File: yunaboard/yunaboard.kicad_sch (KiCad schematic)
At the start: 5 parts, among them J1 USB-C Receptable USB 2.0, U1 ESP32-S3

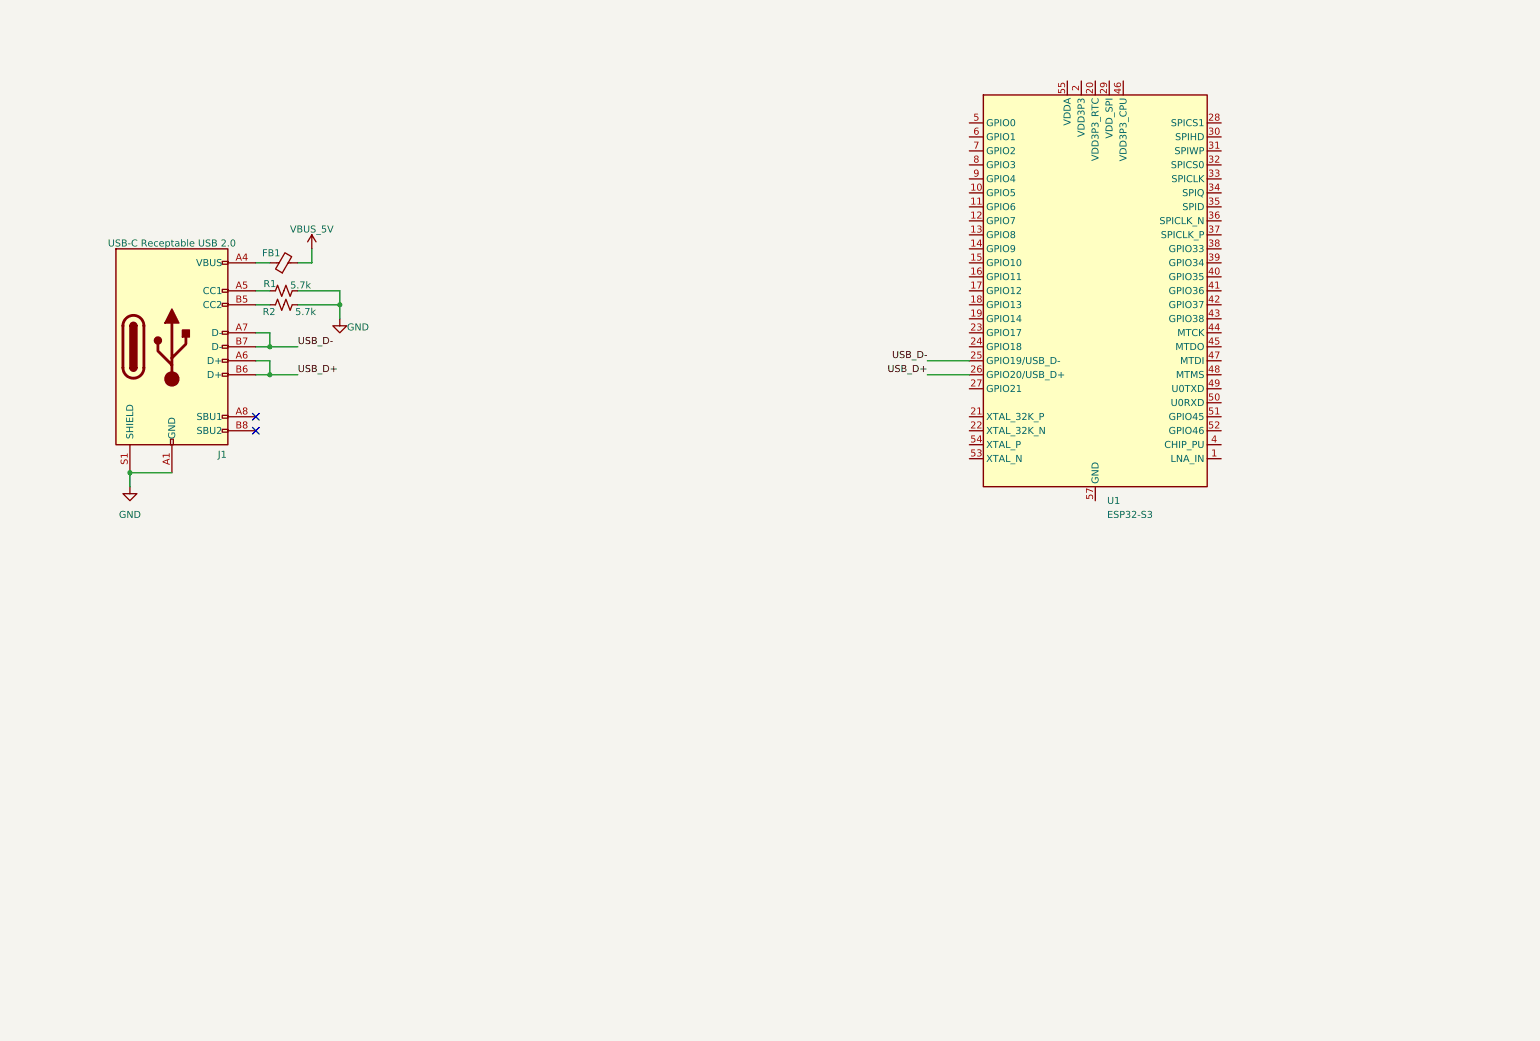
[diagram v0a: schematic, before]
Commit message: Rev 0.1
- Added initial USB-C connections
- Added ESD to USB-C data signals
- Added initial USB-to-UART bridge IC
- Added initial bulk capacitors to power inputs
- Added initial +3.3V LDO regulator
- Added initial ESP32 S3 circuitry
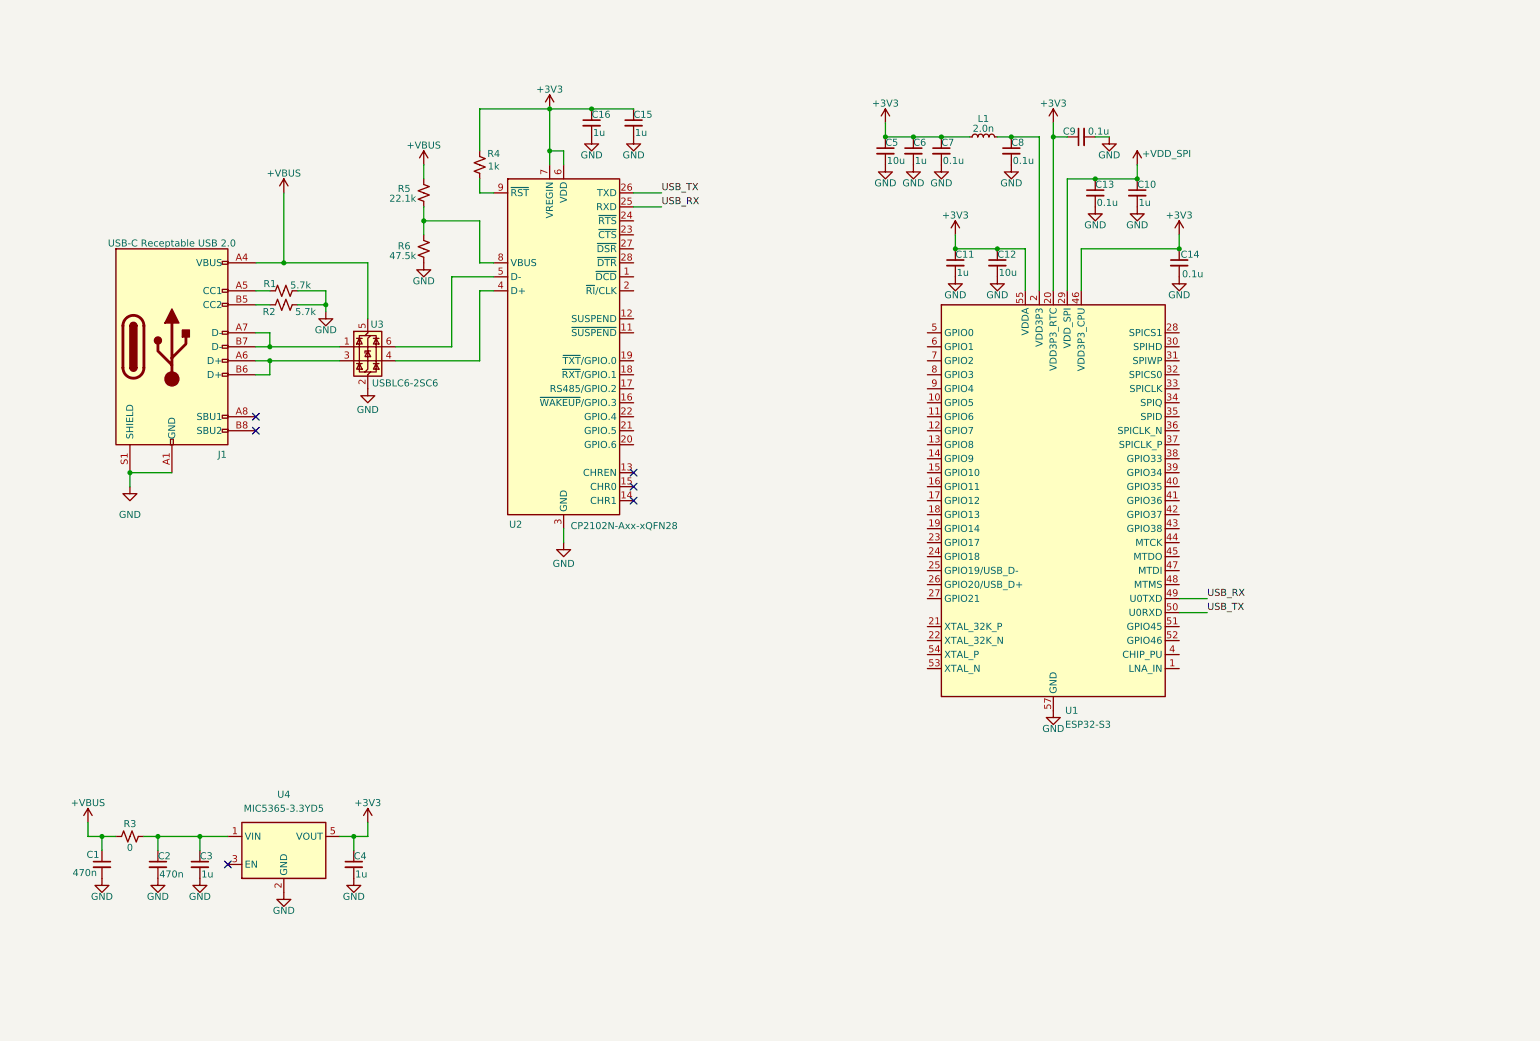
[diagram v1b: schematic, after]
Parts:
- removed FB1: FerriteBead_Small, symbol Device:FerriteBead_Small
- added C1, C2: 470n, symbol Device:C_Small
- added C10, C11, C15, C16, C3, C4, C6: 1u, symbol Device:C_Small
- added C12, C5: 10u, symbol Device:C_Small
- added C13, C14, C7, C8, C9: 0.1u, symbol Device:C_Small
- added L1: 2.0n, symbol Device:L_Small
- added R3: 0, symbol Device:R_Small_US
- added R4: 1k, symbol Device:R_Small_US
- added R5: 22.1k, symbol Device:R_Small_US
- added R6: 47.5k, symbol Device:R_Small_US
- added U2: CP2102N-Axx-xQFN28, Package_DFN_QFN:QFN-28-1EP_5x5mm_P0.5mm_EP3.35x3.35mm, symbol Interface_USB:CP2102N-Axx-xQFN28
- added U3: USBLC6-2SC6, Package_TO_SOT_SMD:SOT-23-6, symbol Power_Protection:USBLC6-2SC6
- added U4: MIC5365-3.3YD5, Package_TO_SOT_SMD:TSOT-23-5, symbol Regulator_Linear:MIC5365-3.3YD5
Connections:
- net GND: now also U1.57 (GND), C1.2, C10.2, C11.2, C12.2, C13.2, C14.2, C15.2, C16.2, C2.2, C3.2, C4.2, C5.2, C6.2, C7.2, C8.2, C9.2, R6.2, U2.29 (GND), U2.3 (GND), U3.2 (GND), U4.2 (GND)
- net +VBUS: now reaches J1.A4 (VBUS), J1.A9 (VBUS), J1.B4 (VBUS), J1.B9 (VBUS)
- net +VBUS: now also C1.1, R3.2, R5.1, U3.5 (VBUS)
- net at U1.2 (VDD3P3), U1.3 (VDD3P3): now also C8.1, L1.2
- net +3V3: now reaches U1.20 (VDD3P3_RTC)
- net +3V3: now also U1.46 (VDD3P3_CPU), U1.55 (VDDA), U1.56 (VDDA), C11.1, C12.1, C14.1, C15.1, C16.1, C4.1, C5.1, C6.1, C7.1, C9.1, L1.1, R4.1, U2.6 (VDD), U2.7 (VREGIN), U4.5 (VOUT)
- net +VDD_SPI: now reaches U1.29 (VDD_SPI)
- net +VDD_SPI: now also C10.1, C13.1
- net USB_RX: now reaches U1.49 (U0TXD)
- net USB_RX: now also U2.25 (RXD)
- net USB_TX: now reaches U1.50 (U0RXD)
- net USB_TX: now also U2.26 (TXD)
- net USB_D+: no longer names the net of J1.A6 (D+), J1.B6 (D+)
- net USB_D+: now also U3.3 (I/O2); no longer U1.26 (GPIO20/USB_D+)
- net USB_D-: no longer names the net of J1.A7 (D-), J1.B7 (D-)
- net USB_D-: now also U3.1 (I/O1); no longer U1.25 (GPIO19/USB_D-)
- new net: C2.1, C3.1, R3.1, U4.1 (VIN)
- new net: U2.4 (D+), U3.4 (I/O2)
- new net: U2.5 (D-), U3.6 (I/O1)
- new net: R5.2, R6.1, U2.8 (VBUS)
- new net: R4.2, U2.9 (~{RST})
- no-connect marks 2 -> 6
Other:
- moved on the sheet: U1

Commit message: Updated schematic
- Placed JTAG tag connect
- Placed initial circuitry to the ESP32 S3 (RF, chip PU)
- Added some labels for better readability
- Found some more documentation for the ESP32
- Added some LEDs to the USB-to-UART bridge
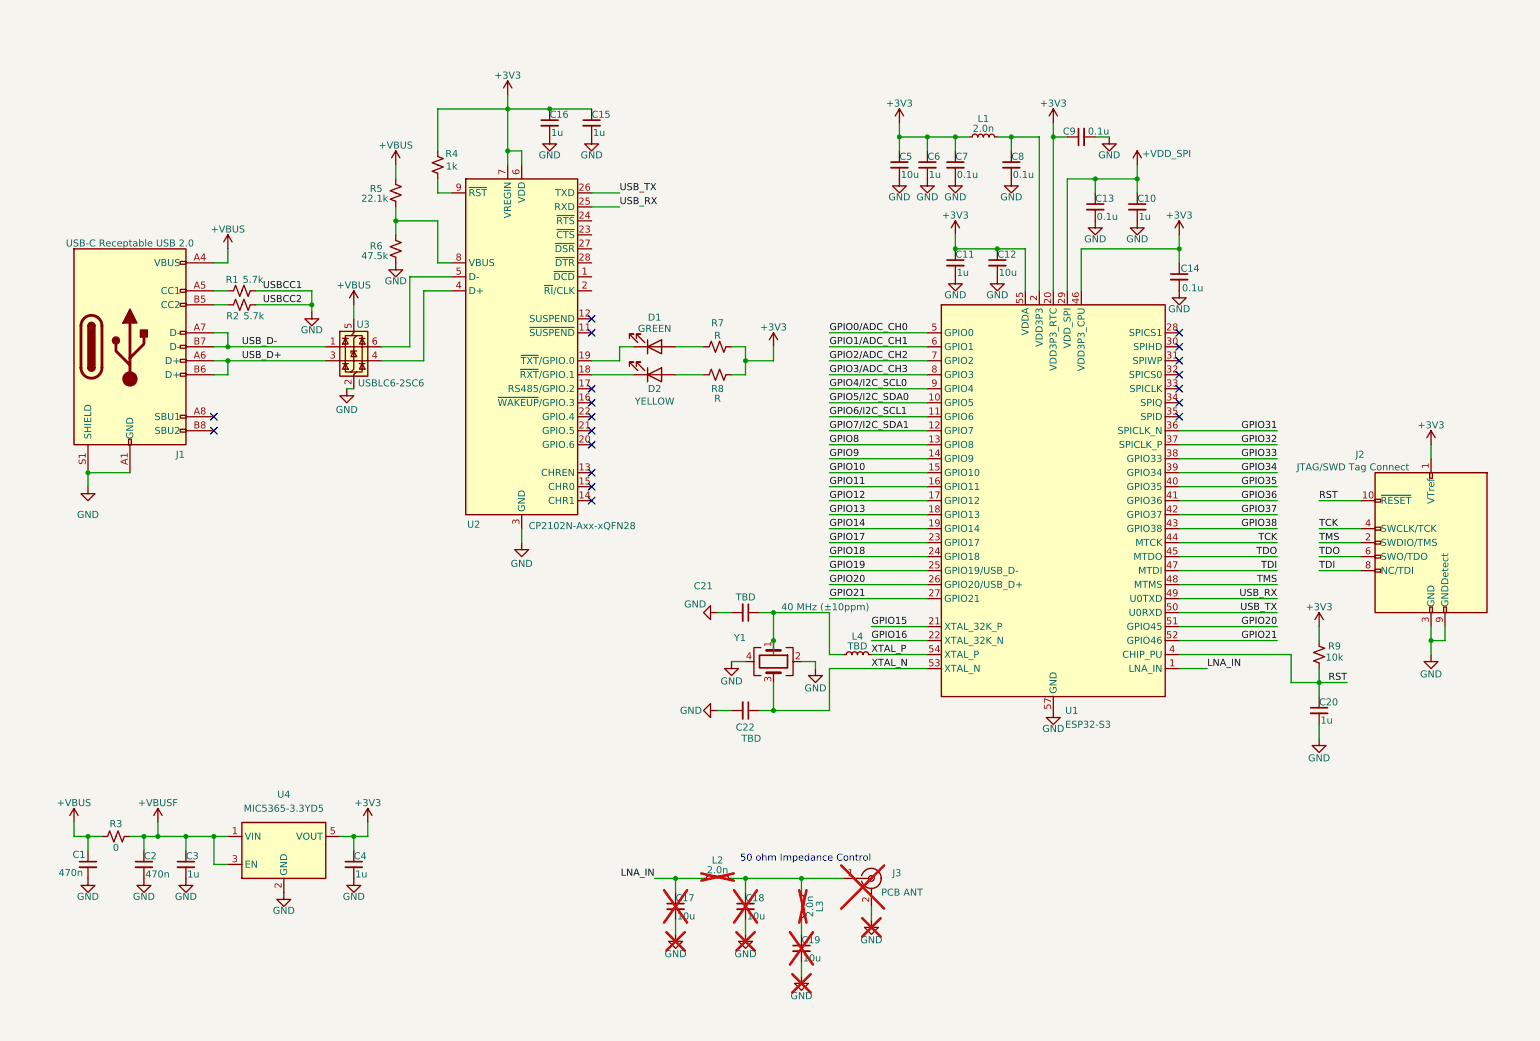
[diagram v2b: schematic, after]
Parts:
- added C17, C18, C19: 10u, symbol Device:C_Small
- added C20: 1u, symbol Device:C_Small
- added C21, C22: TBD, symbol Device:C_Small
- added D1: GREEN, symbol Device:LED
- added D2: YELLOW, symbol Device:LED
- added J2: JTAG/SWD Tag Connect, Connector:Tag-Connect_TC2070-IDC-FP_2x07_P1.27mm_Vertical, symbol Connector:Conn_ARM_JTAG_SWD_10
- added J3: PCB ANT, symbol Connector:Conn_Coaxial
- added L2, L3: 2.0n, symbol Device:L_Small
- added L4: TBD, symbol Device:L_Small
- added R7, R8: R, symbol Device:R_Small_US
- added R9: 10k, symbol Device:R_Small_US
- added Y1: 40 MHz (±10ppm), symbol Device:Crystal_GND24
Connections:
- net +3V3: now also J2.1 (VTref), R7.2, R8.2, R9.2
- net GND: now also C17.2, C18.2, C19.2, C20.2, C21.2, C22.2, J2.3 (GND), J2.5 (GND), J2.9 (GNDDetect), J3.2 (Ext), Y1.2, Y1.4
- net +VBUSF: now reaches C2.1, C3.1, R3.1, U4.1 (VIN)
- net +VBUSF: now also U4.3 (EN)
- net USB_D+: now reaches J1.A6 (D+), J1.B6 (D+), U3.3 (I/O2)
- net USB_D-: now reaches J1.A7 (D-), J1.B7 (D-), U3.1 (I/O1)
- net at U2.18 (~{RXT}/GPIO.1): now also D2.1 (K)
- net at U2.19 (~{TXT}/GPIO.0): now also D1.1 (K)
- net LNA_IN: now reaches U1.1 (LNA_IN)
- net LNA_IN: now also C17.1, L2.1
- net GPIO5/I2C_SDA0: now reaches U1.10 (GPIO5)
- net GPIO6/I2C_SCL1: now reaches U1.11 (GPIO6)
- net GPIO7/I2C_SDA1: now reaches U1.12 (GPIO7)
- net GPIO8: now reaches U1.13 (GPIO8)
- net GPIO9: now reaches U1.14 (GPIO9)
- net GPIO10: now reaches U1.15 (GPIO10)
- net GPIO11: now reaches U1.16 (GPIO11)
- net GPIO12: now reaches U1.17 (GPIO12)
- net GPIO13: now reaches U1.18 (GPIO13)
- net GPIO14: now reaches U1.19 (GPIO14)
- net GPIO15: now reaches U1.21 (XTAL_32K_P)
- net GPIO16: now reaches U1.22 (XTAL_32K_N)
- net GPIO17: now reaches U1.23 (GPIO17)
- net GPIO18: now reaches U1.24 (GPIO18)
- net GPIO19: now reaches U1.25 (GPIO19/USB_D-)
- net GPIO20: now reaches U1.26 (GPIO20/USB_D+)
- net GPIO20: now also U1.51 (GPIO45)
- net GPIO21: now reaches U1.27 (GPIO21)
- net GPIO21: now also U1.52 (GPIO46)
- net GPIO31: now reaches U1.36 (SPICLK_N)
- net GPIO32: now reaches U1.37 (SPICLK_P)
- net GPIO33: now reaches U1.38 (GPIO33)
- net GPIO34: now reaches U1.39 (GPIO34)
- net RST: now reaches U1.4 (CHIP_PU)
- net RST: now also C20.1, J2.10 (~{RESET}), R9.1
- net GPIO35: now reaches U1.40 (GPIO35)
- net GPIO36: now reaches U1.41 (GPIO36)
- net GPIO37: now reaches U1.42 (GPIO37)
- net GPIO38: now reaches U1.43 (GPIO38)
- net TCK: now reaches U1.44 (MTCK)
- net TCK: now also J2.4 (SWCLK/TCK)
- net TDO: now reaches U1.45 (MTDO)
- net TDO: now also J2.6 (SWO/TDO)
- net TDI: now reaches U1.47 (MTDI)
- net TDI: now also J2.8 (NC/TDI)
- net TMS: now reaches U1.48 (MTMS)
- net TMS: now also J2.2 (SWDIO/TMS)
- net GPIO0/ADC_CH0: now reaches U1.5 (GPIO0)
- net XTAL_N: now reaches U1.53 (XTAL_N)
- net XTAL_N: now also C22.1, Y1.3
- net XTAL_P: now reaches U1.54 (XTAL_P)
- net XTAL_P: now also L4.2
- net GPIO1/ADC_CH1: now reaches U1.6 (GPIO1)
- net GPIO2/ADC_CH2: now reaches U1.7 (GPIO2)
- net GPIO3/ADC_CH3: now reaches U1.8 (GPIO3)
- net GPIO4/I2C_SCL0: now reaches U1.9 (GPIO4)
- new net: C18.1, J3.1 (In), L2.2, L3.1
- new net: D1.2 (A), R7.1
- new net: C21.1, L4.1, Y1.1
- new net: C19.1, L3.2
- new net: D2.2 (A), R8.1
- no-connect marks 6 -> 19
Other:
- note added: "50 ohm Impedance Control"
- company: (none) -> Rodolfo Zaragoza
- title: (none) -> YunaBoard
- moved on the sheet: C1, C10, C13, C14, C15, C16, C2, C3, C5, C6, C7, C8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
